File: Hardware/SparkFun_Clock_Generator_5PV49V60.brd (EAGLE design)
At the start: 25.4 x 25.4 mm, 27 parts, among them U1 IDT_5P49V60_CLOCK_GENERATOR, Y2 26MHZ

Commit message: Routes board
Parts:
- moved R1 0.33 mm to (4.93, 18.3), turned to 270 degrees
- moved C1 0.26 mm to (17.4, 15.6)
- moved FB1 0.26 mm to (17.4, 12.8)
- moved C6 0.26 mm to (17.4, 14.2)
- moved R2 0.23 mm to (3.51, 18.3), turned to 270 degrees
- moved J6 0.10 mm to (16.6, 17.8)
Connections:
- new net N$3: JP1.3, R1.1
- net SEL0/SCL: no longer JP1.3, R1.1
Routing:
- net SEL0/SCL: track 0.00 -> 43.8 mm, vias 0 -> 5
- net SEL1/SDA: track 0.00 -> 42.0 mm, vias 0 -> 3
- net SD/OE: track 0.00 -> 22.1 mm, vias 0 -> 2
- net OUT1: track 0.00 -> 13.8 mm, vias 0 -> 1
- net OUT3B: track 0.00 -> 13.2 mm, vias 0 -> 1
- net OUT1B: track 0.00 -> 11.1 mm, vias 0 -> 1
- net OUT3: track 0.00 -> 10.8 mm, vias 0 -> 1
- net OUT2B: track 0.00 -> 9.60 mm, vias 0 -> 1
- net 3.3V: track 53.5 -> 63.1 mm, vias 0 -> 3
- net OUT2: track 0.00 -> 9.28 mm, vias 0 -> 1
- net GND: track 0.00 -> 8.91 mm, vias 0 -> 11
- net CLKINB: track 0.00 -> 5.85 mm
- net N$4: track 0.00 -> 4.19 mm
- net CLKIN: track 0.00 -> 3.24 mm
- net N$3: track 0.00 -> 2.83 mm, vias 0 -> 1
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
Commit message: Adds silk, so much silk
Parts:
- removed Y2: 26MHZ, SparkFun-Clocks:CRYSTAL-SMD-3.2X2.5MM
- added C10, C12: 12pF, SparkFun-Capacitors:0402
- added D1: RED, SparkFun-LED:LED-0603
- added J5: TEST-POINTTP_15TH_THRU, SparkFun-Connectors:TP_15TH
- added LED: JUMPER-SMT_2_NC_TRACE_SILK, SparkFun-Jumpers:SMT-JUMPER_2_NC_TRACE_SILK
- added LOGO1: SFE_LOGO_NAME_FLAME.1_INCH, SparkFun-Aesthetics:SFE_LOGO_NAME_FLAME_.1
- added LOGO2: OSHW-LOGOS, SparkFun-Aesthetics:OSHW-LOGO-S
- added LOGO3: QWIIC_LOGO_4MM, SparkFun-Aesthetics:QWIIC_4MM
- added R3: 1KOHM-0402-1/16W-1%, SparkFun-Resistors:0402
- added U$1: (no value), SparkFun-Aesthetics:QWIIC_4MM
- added U$10: (no value), Every Label:O29
- added U$11: (no value), Every Label:O2B10
- added U$12: (no value), Every Label:O37
- added U$13: (no value), Every Label:O3B8
- added U$14: (no value), Every Label:O4B6
- added U$15: (no value), Every Label:O45
- added U$16: (no value), Every Label:CLOCK_GENERATOR0
- added U$17: (no value), Every Label:5PV49V601
- added U$18, U$2: (no value), Labels:3V3-03
- added U$19, U$3: (no value), Labels:GND-03
- added U$20: (no value), Even more labels:OUT1B4
- added U$21: (no value), Even more labels:OUT2B6
- added U$22: (no value), Even more labels:OUT3B8
- added U$23: (no value), Even more labels:OUT4B10
- added U$24: (no value), Even more labels:OUT13
- added U$25: (no value), Even more labels:OUT25
- added U$26: (no value), Even more labels:OUT37
- added U$27: (no value), Even more labels:OUT49
- added U$28: (no value), Even more labels:SCL1
- added U$29: (no value), Even more labels:SD#OE2
- added U$30: (no value), Even more labels:SDA0
- added U$31, U$34: (no value), Even more labels:CLKB13
- added U$32: (no value), Even more labels:CLK11
- added U$33: (no value), Even more labels:CLK12
- added U$4: (no value), Labels:PWR-()-03
- added U$5: (no value), Every Label:SDA11
- added U$6: (no value), Every Label:SCL10
- added U$7: (no value), Every Label:SD#OE12
- added U$8: (no value), Every Label:O1B12
- added U$9: (no value), Every Label:O111
- added Y1: 16MHz, SparkFun-Clocks:CRYSTAL-SMD-3.2X2.5MM
- J3: device SparkFun-Connectors:SCREWTERMINAL-3.5MM-6 -> SparkFun-Connectors:SCREWTERMINAL-3.5MM-8
- J6: value (none) -> TEST-POINTTP_15TH_THRU; device SparkFun-Connectors:1X02_NO_SILK -> SparkFun-Connectors:TP_15TH
- moved J3 3.56 mm to (0.51, 3.61)
- moved J6 3.54 mm to (19.1, 20.3), turned to 0 degrees
- moved J1 1.27 mm to (3.81, 12.7)
- moved J2 1.27 mm to (21.6, 12.7)
- moved JP1 0.33 mm to (4.42, 17.9)
- moved C5 0.24 mm to (14.5, 9.70)
- moved C4 0.23 mm to (13.1, 9.70)
- moved C3 0.23 mm to (11.7, 9.70)
- moved C9 0.17 mm to (16.0, 10.0)
- moved R1 0.15 mm to (5.08, 18.3)
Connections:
- new net N$5: D1.A, R3.1
- new net N$6: C10.1, U1.P4, Y1.3
- net 3.3V: now also LED.2
- net CLKIN: now also J5.P$1; no longer J6.1
- net CLKINB: now also J6.P$1; no longer J6.2
- net GND: now also C10.2, C12.2, D1.C, Y1.2, Y1.4; no longer Y2.2, Y2.4
- net N$2: now also C12.1, U1.P3, Y1.1; no longer U1.P4, Y2.1
- net N$4: now also LED.1, R3.2; no longer U1.P3, Y2.3
- net OUT1: now also J3.8; no longer J3.6
- net OUT1B: now also J3.7; no longer J3.5
- net OUT2: now also J3.6; no longer J3.4
- net OUT2B: now also J3.5; no longer J3.3
- net OUT3: now also J3.4; no longer J3.2
- net OUT3B: now also J3.3; no longer J3.1
- net OUT4: now also J3.2
- net OUT4B: now also J3.1
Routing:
- net OUT4B: track 0.00 -> 14.6 mm, vias 0 -> 1
- net OUT4: track 0.00 -> 13.7 mm, vias 0 -> 1
- net 3.3V: track 63.1 -> 70.7 mm
- net GND: track 8.91 -> 13.2 mm, vias 11 -> 12
- net SEL1/SDA: track 42.0 -> 46.0 mm
- net N$6: track 0.00 -> 3.90 mm
- net SEL0/SCL: track 43.8 -> 47.4 mm
- net N$2: track 2.42 -> 5.64 mm
- net CLKIN: track 3.24 -> 5.68 mm
- net OUT3B: track 13.2 -> 11.2 mm
- net SD/OE: track 22.1 -> 24.0 mm
- net OUT1B: track 11.1 -> 12.8 mm
- net OUT1: track 13.8 -> 15.4 mm
- net OUT2: track 9.28 -> 10.9 mm
- net CLKINB: track 5.85 -> 7.42 mm
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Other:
- board size 25.4 x 25.4 mm -> 27.9 x 25.4 mm
- board text added: "Units in Inches"

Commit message: Adds a few (probably) unnecessary stitching vias
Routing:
- net GND: vias 12 -> 18
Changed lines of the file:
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@@
 <wire x1="15.24" y1="18.0848" x2="15.24" y2="18.796" width="0.508" layer="1"/>
 <contactref element="D1" pad="C"/>
+<via x="7.6962" y="10.2108" extent="1-16" drill="0.381"/>
+<via x="8.9154" y="8.8646" extent="1-16" drill="0.381"/>
+<via x="10.3124" y="8.8646" extent="1-16" drill="0.381"/>
+<via x="11.9634" y="6.0706" extent="1-16" drill="0.381"/>
+<via x="13.1826" y="6.0452" extent="1-16" drill="0.381"/>
+<via x="19.9136" y="6.4516" extent="1-16" drill="0.381"/>
 </signal>
 <signal name="3.3V">
@@
 <wire x1="9.834" y1="10.2828" x2="8.3312" y2="11.7856" width="0.254" layer="1"/>
 <wire x1="8.3312" y1="11.7856" x2="8.3312" y2="13.2334" width="0.254" layer="1"/>
-<wire x1="8.3312" y1="13.2334" x2="8.3312" y2="14.224" width="0.254" layer="1"/>
+<wire x1="8.3312" y1="14.224" x2="8.3312" y2="13.2334" width="0.254" layer="1"/>
 <wire x1="8.3312" y1="14.224" x2="8.3312" y2="15.3458" width="0.254" layer="1"/>
 <wire x1="8.3312" y1="15.3458" x2="8.4286" y2="15.4432" width="0.254" layer="1"/>
@@
 <wire x1="10.16" y1="14.228" x2="10.156" y2="14.224" width="0.254" layer="1"/>
 <wire x1="10.156" y1="14.224" x2="8.3312" y2="14.224" width="0.254" layer="1"/>
-<wire x1="3.810003125" y1="13.2" x2="8.2978" y2="13.2" width="0.254" layer="1"/>
 <wire x1="8.2978" y1="13.2" x2="8.3312" y2="13.2334" width="0.254" layer="1"/>
 <wire x1="8.4286" y1="18.1864" x2="8.382" y2="18.233" width="0.254" layer="1"/>
@@
 <wire x1="22.4536" y1="16.0782" x2="22.4536" y2="16.9164" width="0.2032" layer="16"/>
 <wire x1="23.4188" y1="15.113" x2="22.4536" y2="16.0782" width="0.2032" layer="16"/>
-<wire x1="3.810003125" y1="13.2" x2="3.81" y2="13.2" width="0" layer="19" extent="1-1"/>
+<wire x1="8.2978" y1="13.2" x2="3.81" y2="13.2" width="0.2032" layer="1"/>
 </signal>
 <signal name="SEL1/SDA">
@@
 <wire x1="20.6502" y1="13.4794" x2="20.9296" y2="13.2" width="0.2032" layer="1"/>
 <wire x1="20.6502" y1="15.2908" x2="20.6502" y2="13.4794" width="0.2032" layer="1"/>
-<wire x1="3.4036" y1="17.581" x2="3.5052" y2="17.6826" width="0.254" layer="1"/>
 <wire x1="2.1376" y1="12.6024" x2="2.1376" y2="16.315" width="0.2032" layer="1"/>
 <wire x1="2.1376" y1="16.315" x2="3.5052" y2="17.6826" width="0.2032" layer="1"/>
@@
 <wire x1="14.9406" y1="13.228" x2="15.5194" y2="12.6492" width="0.2032" layer="1"/>
 <via x="15.5194" y="12.6492" extent="1-16" drill="0.381"/>
-<wire x1="15.5194" y1="12.6492" x2="15.6002" y2="12.5684" width="0.2032" layer="16"/>
 <contactref element="J3" pad="7"/>
 <wire x1="15.5194" y1="12.6492" x2="15.5194" y2="9.5758" width="0.2032" layer="16"/>
@@
 <wire x1="12.5476" y1="10.9982" x2="12.8016" y2="11.2522" width="0.2032" layer="16"/>
 <contactref element="J3" pad="5"/>
-<wire x1="14.508" y1="3.6276" x2="14.508" y2="3.6068" width="0.2032" layer="16"/>
 <wire x1="14.508" y1="3.6068" x2="12.5476" y2="5.5672" width="0.2032" layer="16"/>
 <wire x1="12.5476" y1="5.5672" x2="12.5476" y2="10.9982" width="0.2032" layer="16"/>

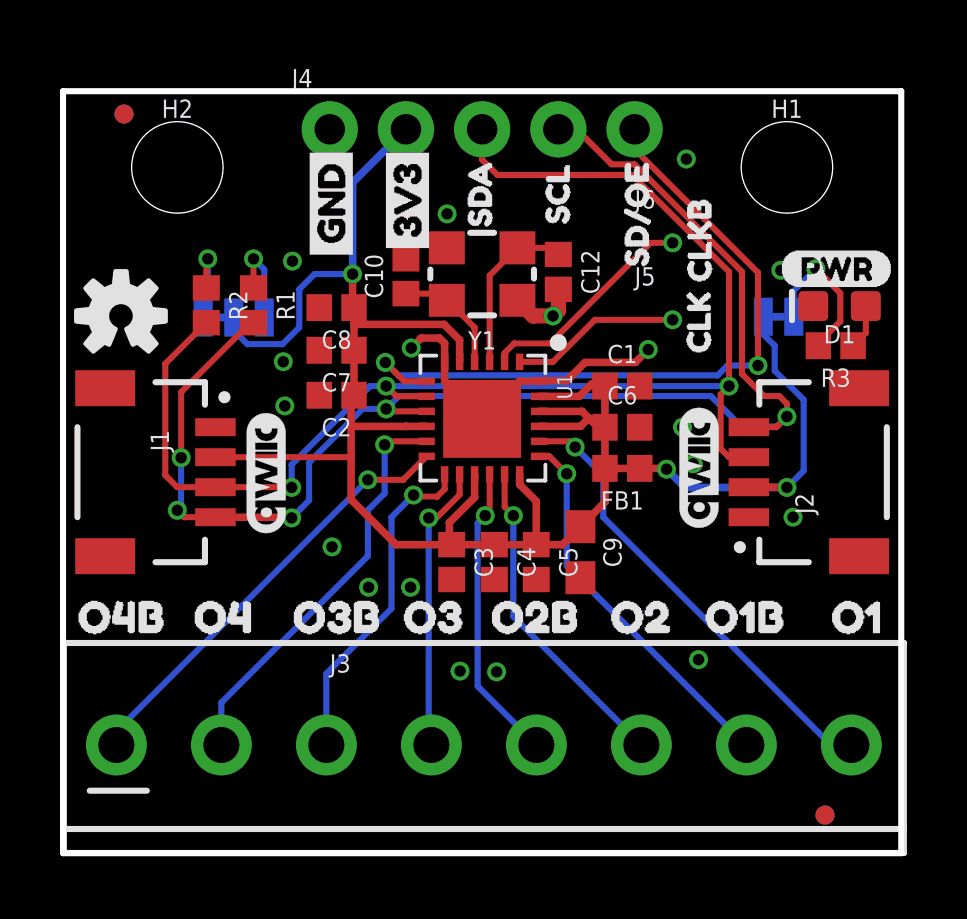
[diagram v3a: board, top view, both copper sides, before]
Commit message: Adds silk to jumpers and adds smaller diameter through holes for clock signals
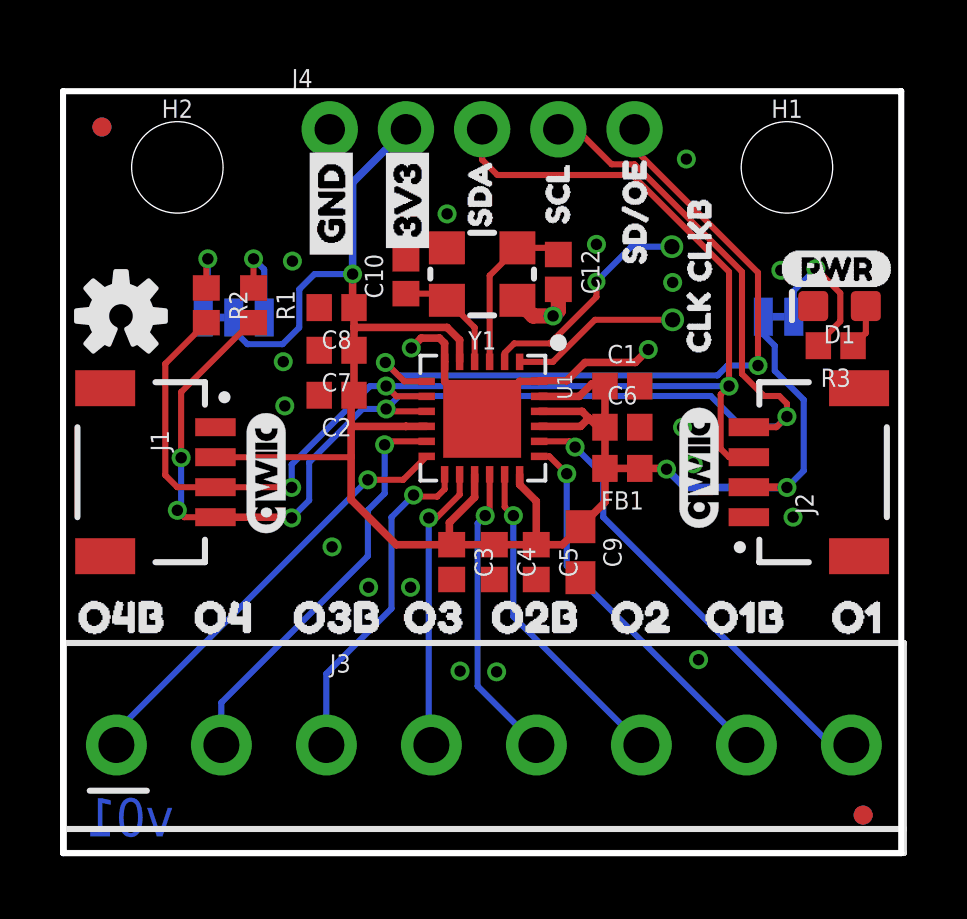
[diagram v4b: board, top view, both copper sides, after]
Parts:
- removed J5, J6: TEST-POINTTP_15TH_THRU, SparkFun-Connectors:TP_15TH
- added J7, J8: (no value), SparkFun-Connectors:1X01_SMALL
- added U$35: (no value), Labels:I_SUPER2_C-()-03
- added U$36: (no value), led:LED0
- moved FD3 1.27 mm to (25.4, 1.27)
- moved FD4 1.27 mm to (25.4, 1.27)
- moved FD1 0.85 mm to (0.03, 24.2)
- moved FD2 0.85 mm to (0.03, 24.2)
- moved U$7 0.11 mm to (17.8, 18.9)
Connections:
- net CLKIN: now also J8.P$1; no longer J5.P$1
- net CLKINB: now also J7.P$1; no longer J6.P$1
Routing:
- net CLKINB: track 7.42 -> 7.64 mm, vias 0 -> 1
- net GND: vias 18 -> 20
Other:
- board text added: "v01"
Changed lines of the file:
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@@
 <drawing>
 <settings>
-<setting alwaysvectorfont="no"/>
+<setting alwaysvectorfont="yes"/>
 <setting verticaltext="up"/>
 </settings>
@@
 <text x="4.572" y="-3.81" size="1.778" layer="47" font="vector">Units in Inches</text>
 <dimension x1="2.54" y1="22.86" x2="22.86" y2="22.86" x3="12.7" y3="26.162" textsize="1.778" layer="47" dtype="horizontal" unit="inch"/>
+<text x="-0.508" y="1.8288" size="1.27" layer="16" font="vector" ratio="12" rot="MR180">v01</text>
 </plain>
 <attributes>
@@
 <attribute name="VALUE" x="2.54" y="21.209" size="0.6096" layer="27" font="vector" ratio="20" align="top-center"/>
 </element>
-<element name="FD1" library="SparkFun-Aesthetics" package="FIDUCIAL-MICRO" value="FIDUCIALUFIDUCIAL" x="0.762" y="24.638" smashed="yes"/>
-<element name="FD2" library="SparkFun-Aesthetics" package="FIDUCIAL-MICRO" value="FIDUCIALUFIDUCIAL" x="0.762" y="24.638" smashed="yes" rot="MR0"/>
-<element name="FD3" library="SparkFun-Aesthetics" package="FIDUCIAL-MICRO" value="FIDUCIALUFIDUCIAL" x="24.13" y="1.27" smashed="yes" rot="MR0"/>
-<element name="FD4" library="SparkFun-Aesthetics" package="FIDUCIAL-MICRO" value="FIDUCIALUFIDUCIAL" x="24.13" y="1.27" smashed="yes"/>
+<element name="FD1" library="SparkFun-Aesthetics" package="FIDUCIAL-MICRO" value="FIDUCIALUFIDUCIAL" x="0.0254" y="24.2062" smashed="yes"/>
+<element name="FD2" library="SparkFun-Aesthetics" package="FIDUCIAL-MICRO" value="FIDUCIALUFIDUCIAL" x="0.0254" y="24.2062" smashed="yes" rot="MR0"/>
+<element name="FD3" library="SparkFun-Aesthetics" package="FIDUCIAL-MICRO" value="FIDUCIALUFIDUCIAL" x="25.4" y="1.27" smashed="yes" rot="MR0"/>
+<element name="FD4" library="SparkFun-Aesthetics" package="FIDUCIAL-MICRO" value="FIDUCIALUFIDUCIAL" x="25.4" y="1.27" smashed="yes"/>
 <element name="JP1" library="SparkFun-Jumpers" package="SMT-JUMPER_3_2-NC_TRACE_SILK" value="JUMPER-SMT_3_2-NC_TRACE_SILK" x="4.4196" y="17.8562" smashed="yes" rot="MR180">
 <attribute name="NAME" x="4.4196" y="16.7132" size="0.6096" layer="26" font="vector" ratio="20" rot="MR180" align="bottom-center"/>
@@
 <attribute name="PROD_ID" value="" x="10.16" y="19.232" size="1.778" layer="27" font="vector" rot="R90" display="off"/>
 <attribute name="VALUE" value="12pF" x="10.922" y="19.232" size="0.6096" layer="27" font="vector" ratio="20" rot="R90" align="top-center"/>
-</element>
-<element name="J5" library="SparkFun-Connectors" package="TP_15TH" value="TEST-POINTTP_15TH_THRU" x="19.05" y="17.78" smashed="yes">
-<attribute name="NAME" x="17.78" y="18.923" size="0.6096" layer="25" font="vector" ratio="20"/>
-<attribute name="VALUE" x="17.78" y="16.002" size="0.6096" layer="27" font="vector" ratio="20"/>
-</element>
-<element name="J6" library="SparkFun-Connectors" package="TP_15TH" value="TEST-POINTTP_15TH_THRU" x="19.05" y="20.3454" smashed="yes">
-<attribute name="NAME" x="17.78" y="21.4884" size="0.6096" layer="25" font="vector" ratio="20"/>
-<attribute name="VALUE" x="17.78" y="18.5674" size="0.6096" layer="27" font="vector" ratio="20"/>
 </element>
 <element name="D1" library="SparkFun-LED" package="LED-0603" value="RED" x="24.6126" y="18.2372" smashed="yes" rot="R180">
@@
 <element name="U$5" library="Every Label" package="SDA11" value="" x="12.6238" y="20.193" smashed="yes" rot="R90"/>
 <element name="U$6" library="Every Label" package="SCL10" value="" x="15.2146" y="20.2946" smashed="yes" rot="R90"/>
-<element name="U$7" library="Every Label" package="SD#OE12" value="" x="17.8562" y="18.8722" smashed="yes" rot="R90"/>
+<element name="U$7" library="Every Label" package="SD#OE12" value="" x="17.78" y="18.9484" smashed="yes" rot="R90"/>
 <element name="U$8" library="Every Label" package="O1B12" value="" x="19.2278" y="7.874" smashed="yes"/>
 <element name="U$9" library="Every Label" package="O111" value="" x="23.4442" y="7.874" smashed="yes"/>
@@
 <element name="U$33" library="Even more labels" package="CLK12" value="" x="19.9136" y="16.002" smashed="yes" rot="R90"/>
 <element name="U$34" library="Even more labels" package="CLKB13" value="" x="19.939" y="18.3642" smashed="yes" rot="R90"/>
+<element name="U$35" library="Labels" package="I_SUPER2_C-()-03" value="" x="5.7658" y="16.002" smashed="yes" rot="MR0"/>
+<element name="U$36" library="led" package="LED0" value="" x="24.5618" y="16.002" smashed="yes" rot="MR0"/>
+<element name="J7" library="SparkFun-Connectors" package="1X01_SMALL" value="" x="19.0246" y="20.2184" smashed="yes"/>
+<element name="J8" library="SparkFun-Connectors" package="1X01_SMALL" value="" x="19.05" y="17.78" smashed="yes"/>
 </elements>
 <signals>
@@
 <via x="13.1826" y="6.0452" extent="1-16" drill="0.381"/>
 <via x="19.9136" y="6.4516" extent="1-16" drill="0.381"/>
+<via x="19.05" y="19.0246" extent="1-16" drill="0.381"/>
+<via x="16.51" y="20.2946" extent="1-16" drill="0.381"/>
 </signal>
 <signal name="3.3V">
@@
 <contactref element="C5" pad="1"/>
 <contactref element="FB1" pad="2"/>
-<wire x1="8.4286" y1="18.1864" x2="8.4286" y2="17.6276" width="0.254" layer="1"/>
-<wire x1="8.4286" y1="17.6276" x2="8.4286" y2="16.764" width="0.254" layer="1"/>
+<wire x1="8.4286" y1="18.1864" x2="8.4286" y2="17.526" width="0.254" layer="1"/>
+<wire x1="8.4286" y1="17.526" x2="8.4286" y2="16.764" width="0.254" layer="1"/>
 <wire x1="14.5034" y1="10.2828" x2="15.3764" y2="10.2828" width="0.254" layer="1"/>
 <wire x1="15.3764" y1="10.2828" x2="15.9766" y2="10.883" width="0.254" layer="1"/>
@@
 <wire x1="15.9806" y1="14.228" x2="16.256" y2="14.5034" width="0.254" layer="1"/>
 <wire x1="11.95" y1="16.378" x2="11.95" y2="17.1076" width="0.254" layer="1"/>
-<wire x1="11.43" y1="17.6276" x2="8.4286" y2="17.6276" width="0.254" layer="1"/>
-<wire x1="11.95" y1="17.1076" x2="11.43" y2="17.6276" width="0.254" layer="1"/>
+<wire x1="11.5316" y1="17.526" x2="8.4286" y2="17.526" width="0.254" layer="1"/>
+<wire x1="11.95" y1="17.1076" x2="11.5316" y2="17.526" width="0.254" layer="1"/>
 <wire x1="12.45" y1="12.628" x2="12.45" y2="11.8618" width="0.254" layer="1"/>
 <wire x1="12.45" y1="11.8618" x2="11.6078" y2="11.0196" width="0.254" layer="1"/>
@@
 <signal name="CLKIN">
 <contactref element="U1" pad="P1"/>
-<contactref element="J5" pad="P$1"/>
 <wire x1="13.95" y1="16.378" x2="15.0572" y2="16.378" width="0.2032" layer="1"/>
 <wire x1="15.0572" y1="16.378" x2="16.4592" y2="17.78" width="0.2032" layer="1"/>
+<contactref element="J8" pad="P$1"/>
 <wire x1="16.4592" y1="17.78" x2="19.05" y2="17.78" width="0.2032" layer="1"/>
 </signal>
@@
 <contactref element="U1" pad="P2"/>
 <wire x1="13.7668" y1="16.9926" x2="14.9606" y2="16.9926" width="0.2032" layer="1"/>
-<wire x1="14.9606" y1="16.9926" x2="18.3134" y2="20.3454" width="0.2032" layer="1"/>
 <wire x1="13.45" y1="16.6758" x2="13.45" y2="16.378" width="0.2032" layer="1"/>
 <wire x1="13.7668" y1="16.9926" x2="13.45" y2="16.6758" width="0.2032" layer="1"/>
-<contactref element="J6" pad="P$1"/>
-<wire x1="18.3134" y1="20.3454" x2="19.05" y2="20.3454" width="0.2032" layer="1"/>
+<contactref element="J7" pad="P$1"/>
+<wire x1="14.9606" y1="16.9926" x2="16.51" y2="18.542" width="0.2032" layer="1"/>
+<wire x1="16.51" y1="18.542" x2="16.51" y2="19.05" width="0.2032" layer="1"/>
+<via x="16.51" y="19.05" extent="1-16" drill="0.35"/>
+<wire x1="16.51" y1="19.05" x2="17.6784" y2="20.2184" width="0.2032" layer="16"/>
+<wire x1="17.6784" y1="20.2184" x2="19.0246" y2="20.2184" width="0.2032" layer="16"/>
 </signal>
 <signal name="N$1">
